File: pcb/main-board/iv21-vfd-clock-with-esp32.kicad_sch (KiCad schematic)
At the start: 30 parts, among them J1 Conn_02x10_Odd_Even, J2 4328, J4 Barrel_Jack_MountingPin, Q3 MMBT3904, Q4 MMBT3904, SW1 SW_SPST, SW2 SW_SPST, U1 MAX6921AQI_, U2 MOUDLE-SEEEDUINO-XIAO-ESP32C3, U4 MCP3221, U6 AZ1117-5.0

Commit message: PDF of schematic.
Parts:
- removed R1: 10K, Resistor_SMD:R_0805_2012Metric_Pad1.20x1.40mm_HandSolder, symbol Device:R_US
- R8: value 62 -> 2K
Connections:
- net at U2.3 (PA10_A2_D2): now also Q4.1 (B)
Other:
- moved on the sheet: C1, C2
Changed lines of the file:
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@@
 	)
 	(junction
-		(at 208.28 21.59)
+		(at 143.51 171.45)
 		(diameter 0)
 		(color 0 0 0 0)
 	)
 	(junction
-		(at 144.78 171.45)
+		(at 208.28 21.59)
 		(diameter 0)
 		(color 0 0 0 0)
@@
 	)
 	(junction
-		(at 139.7 171.45)
+		(at 156.21 171.45)
 		(diameter 0)
 		(color 0 0 0 0)
 	)
 	(junction
-		(at 151.13 171.45)
+		(at 148.59 171.45)
 		(diameter 0)
 		(color 0 0 0 0)
@@
 	(wire
 		(pts
+			(xy 143.51 171.45) (xy 148.59 171.45)
+		)
+		(stroke
+			(width 0)
+			(type default)
+		)
+	)
+	(wire
+		(pts
 			(xy 41.91 68.58) (xy 67.31 68.58)
 		)
@@
 	(wire
 		(pts
-			(xy 146.05 161.29) (xy 151.13 161.29)
+			(xy 146.05 161.29) (xy 156.21 161.29)
 		)
 		(stroke
@@
 	(wire
 		(pts
-			(xy 41.91 128.27) (xy 143.51 128.27)
+			(xy 41.91 128.27) (xy 152.4 128.27)
 		)
 		(stroke
@@
 	(wire
 		(pts
-			(xy 151.13 171.45) (xy 151.13 161.29)
+			(xy 156.21 171.45) (xy 156.21 161.29)
 		)
 		(stroke
@@
 	(wire
 		(pts
-			(xy 127 171.45) (xy 139.7 171.45)
+			(xy 127 171.45) (xy 143.51 171.45)
 		)
 		(stroke
@@
 	(wire
 		(pts
-			(xy 227.33 85.09) (xy 231.14 85.09)
+			(xy 148.59 171.45) (xy 156.21 171.45)
 		)
 		(stroke
@@
 	(wire
 		(pts
-			(xy 116.84 60.96) (xy 120.65 60.96)
+			(xy 227.33 85.09) (xy 231.14 85.09)
 		)
 		(stroke
@@
 	(wire
 		(pts
-			(xy 194.31 64.77) (xy 177.8 64.77)
+			(xy 116.84 60.96) (xy 120.65 60.96)
 		)
 		(stroke
@@
 	(wire
 		(pts
-			(xy 55.88 96.52) (xy 134.62 96.52)
+			(xy 194.31 64.77) (xy 177.8 64.77)
 		)
 		(stroke
@@
 	(wire
 		(pts
-			(xy 64.77 43.18) (xy 63.5 43.18)
+			(xy 55.88 96.52) (xy 134.62 96.52)
 		)
 		(stroke
@@
 	(wire
 		(pts
-			(xy 104.14 139.7) (xy 114.3 139.7)
+			(xy 64.77 43.18) (xy 63.5 43.18)
 		)
 		(stroke
@@
 	(wire
 		(pts
-			(xy 58.42 80.01) (xy 67.31 80.01)
+			(xy 104.14 139.7) (xy 114.3 139.7)
 		)
 		(stroke
@@
 	(wire
 		(pts
-			(xy 152.4 128.27) (xy 151.13 128.27)
+			(xy 58.42 80.01) (xy 67.31 80.01)
 		)
 		(stroke
@@
 	(wire
 		(pts
-			(xy 151.13 171.45) (xy 144.78 171.45)
-		)
-		(stroke
-			(width 0)
-			(type default)
-		)
-	)
-	(wire
-		(pts
 			(xy 33.02 83.82) (xy 33.02 88.9)
 		)
@@
 	(wire
 		(pts
-			(xy 144.78 163.83) (xy 144.78 171.45)
+			(xy 148.59 163.83) (xy 148.59 171.45)
 		)
 		(stroke
@@
 	(wire
 		(pts
-			(xy 139.7 171.45) (xy 144.78 171.45)
-		)
-		(stroke
-			(width 0)
-			(type default)
-		)
-	)
-	(wire
-		(pts
 			(xy 16.51 63.5) (xy 16.51 69.85)
 		)
@@
 	(wire
 		(pts
-			(xy 144.78 163.83) (xy 143.51 163.83)
-		)
-		(stroke
-			(width 0)
-			(type default)
-		)
-	)
-	(wire
-		(pts
 			(xy 234.95 72.39) (xy 234.95 52.07)
 		)
@@
 	)
 	(label "VPP"
-		(at 144.78 166.37 0)
+		(at 148.59 166.37 0)
 		(effects
 			(font
@@
 			)
 		)
-		(property "Value" "62"
+		(property "Value" "2K"
 			(at 255.27 58.4199 0)
 			(effects
@@
 	(symbol
 		(lib_id "Device:C_Polarized_US")
-		(at 139.7 175.26 0)
+		(at 143.51 175.26 0)
 		(unit 1)
 		(exclude_from_sim no)
@@
 		(dnp no)
 		(property "Reference" "C1"
-			(at 142.494 173.99 0)
+			(at 146.304 173.99 0)
 			(effects
 				(font
@@
 		)
 		(property "Value" "33uF"
-			(at 142.494 176.53 0)
+			(at 146.304 176.53 0)
 			(effects
 				(font
@@
 		)
 		(property "Footprint" "Capacitor_SMD:CP_Elec_8x10.5"
-			(at 139.7 175.26 0)
+			(at 143.51 175.26 0)
 			(effects
 				(font
@@
 		)
 		(property "Datasheet" "~"
-			(at 139.7 175.26 0)
+			(at 143.51 175.26 0)
 			(effects
 				(font
@@
 		)
 		(property "Description" "Polarized capacitor, US symbol"
-			(at 139.7 175.26 0)
+			(at 143.51 175.26 0)
 			(effects
 				(font
@@
 	(symbol
 		(lib_id "power:GND")
-		(at 151.13 179.07 0)
+		(at 156.21 179.07 0)
 		(unit 1)
 		(exclude_from_sim no)
@@
 		(fields_autoplaced yes)
 		(property "Reference" "#PWR010"
-			(at 151.13 185.42 0)
+			(at 156.21 185.42 0)
 			(effects
 				(font
@@
 		)
 		(property "Value" "GND"
-			(at 151.13 184.15 0)
+			(at 156.21 184.15 0)
 			(effects
 				(font
@@
 		)
 		(property "Footprint" ""
-			(at 151.13 179.07 0)
+			(at 156.21 179.07 0)
 			(effects
 				(font
@@
 		)
 		(property "Datasheet" ""
-			(at 151.13 179.07 0)
+			(at 156.21 179.07 0)
 			(effects
 				(font
@@
 		)
 		(property "Description" "Power symbol creates a global label with name \"GND\" , ground"
-			(at 151.13 179.07 0)
+			(at 156.21 179.07 0)
 			(effects
 				(font
@@
 	(symbol
 		(lib_id "power:GND")
-		(at 139.7 179.07 0)
+		(at 143.51 179.07 0)
 		(unit 1)
 		(exclude_from_sim no)
@@
 		(fields_autoplaced yes)
 		(property "Reference" "#PWR09"
-			(at 139.7 185.42 0)
+			(at 143.51 185.42 0)
 			(effects
 				(font
@@
 		)
 		(property "Value" "GND"
-			(at 139.7 184.15 0)
+			(at 143.51 184.15 0)
 			(effects
 				(font
@@
 		)
 		(property "Footprint" ""
-			(at 139.7 179.07 0)
+			(at 143.51 179.07 0)
 			(effects
 				(font
@@
 		)
 		(property "Datasheet" ""
-			(at 139.7 179.07 0)
+			(at 143.51 179.07 0)
 			(effects
 				(font
@@
 		)
 		(property "Description" "Power symbol creates a global label with name \"GND\" , ground"
-			(at 139.7 179.07 0)
+			(at 143.51 179.07 0)
 			(effects
 				(font
@@
 	)
 	(symbol
-		(lib_id "Device:R_US")
-		(at 147.32 128.27 90)
-		(unit 1)
-		(exclude_from_sim no)
-		(in_bom yes)
-		(on_board yes)
-		(dnp no)
-		(fields_autoplaced yes)
-		(property "Reference" "R1"
-			(at 147.32 121.92 90)
-			(effects
-				(font
-					(size 1.27 1.27)
-				)
-			)
-		)
-		(property "Value" "10K"
-			(at 147.32 124.46 90)
-			(effects
-				(font
-					(size 1.27 1.27)
-				)
-			)
-		)
-		(property "Footprint" "Resistor_SMD:R_0805_2012Metric_Pad1.20x1.40mm_HandSolder"
-			(at 147.574 127.254 90)
-			(effects
-				(font
-					(size 1.27 1.27)
-				)
-				(hide yes)
-			)
-		)
-		(property "Datasheet" "~"
-			(at 147.32 128.27 0)
-			(effects
-				(font
-					(size 1.27 1.27)
-				)
-				(hide yes)
-			)
-		)
-		(property "Description" "Resistor, US symbol"
-			(at 147.32 128.27 0)
-			(effects
-				(font
-					(size 1.27 1.27)
-				)
-				(hide yes)
-			)
-		)
-		(pin "1"
-		)
-		(pin "2"
-		)
-		(instances
-			(project ""
-				(path "/f4ccf12f-2c39-4319-adc8-75ef731d1807"
-					(reference "R1")
-					(unit 1)
-				)
-			)
-		)
-	)
-	(symbol
 		(lib_id "power:GND")
 		(at 29.21 55.88 0)
@@
 	(symbol
 		(lib_id "Device:C_Polarized_US")
-		(at 151.13 175.26 0)
+		(at 156.21 175.26 0)
 		(unit 1)
 		(exclude_from_sim no)
@@
 		(dnp no)
 		(property "Reference" "C2"
-			(at 154.432 173.99 0)
+			(at 159.512 173.99 0)
 			(effects
 				(font
@@
 		)
 		(property "Value" "0.1uF"
-			(at 154.432 176.276 0)
+			(at 159.512 176.276 0)
 			(effects
 				(font
@@
 		)
 		(property "Footprint" "Resistor_SMD:R_0805_2012Metric_Pad1.20x1.40mm_HandSolder"
-			(at 151.13 175.26 0)
+			(at 156.21 175.26 0)
 			(effects
 				(font
@@
 		)
 		(property "Datasheet" "~"
-			(at 151.13 175.26 0)
+			(at 156.21 175.26 0)
 			(effects
 				(font
@@
 		)
 		(property "Description" "Polarized capacitor, US symbol"
-			(at 151.13 175.26 0)
+			(at 156.21 175.26 0)
 			(effects
 				(font

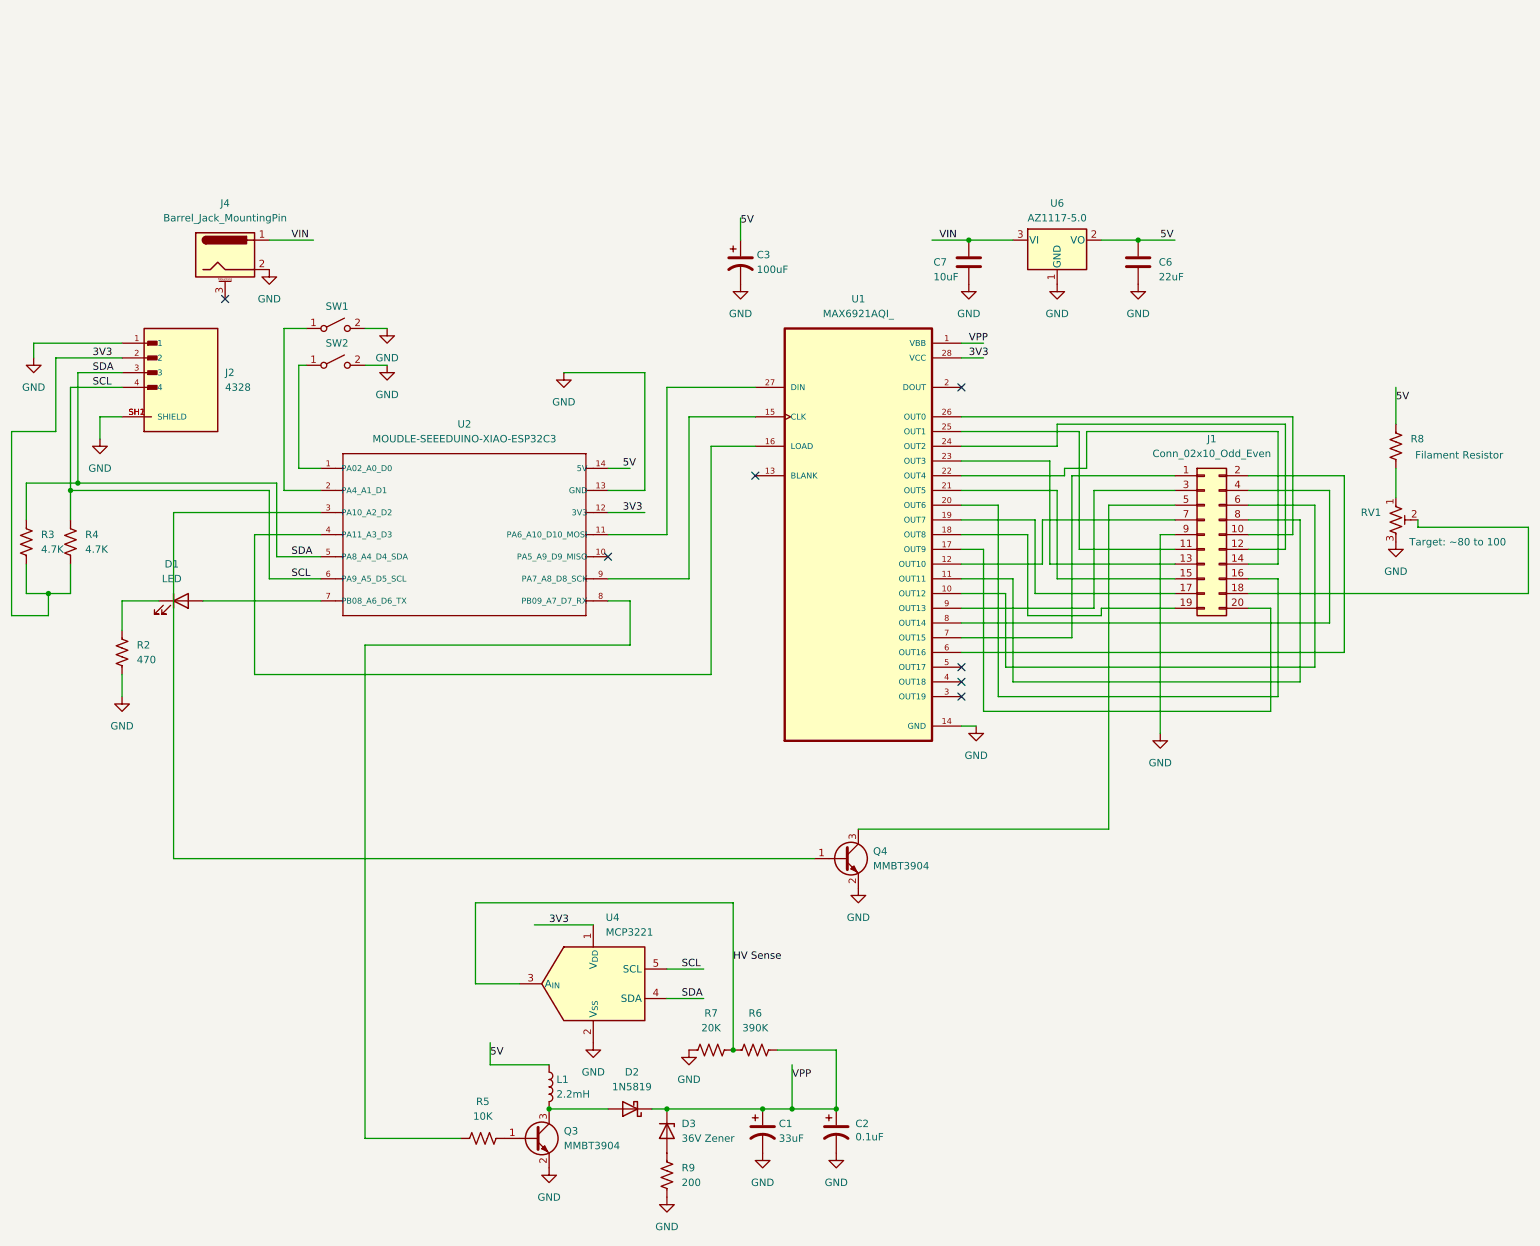
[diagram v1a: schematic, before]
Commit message: Voltage regulation update.
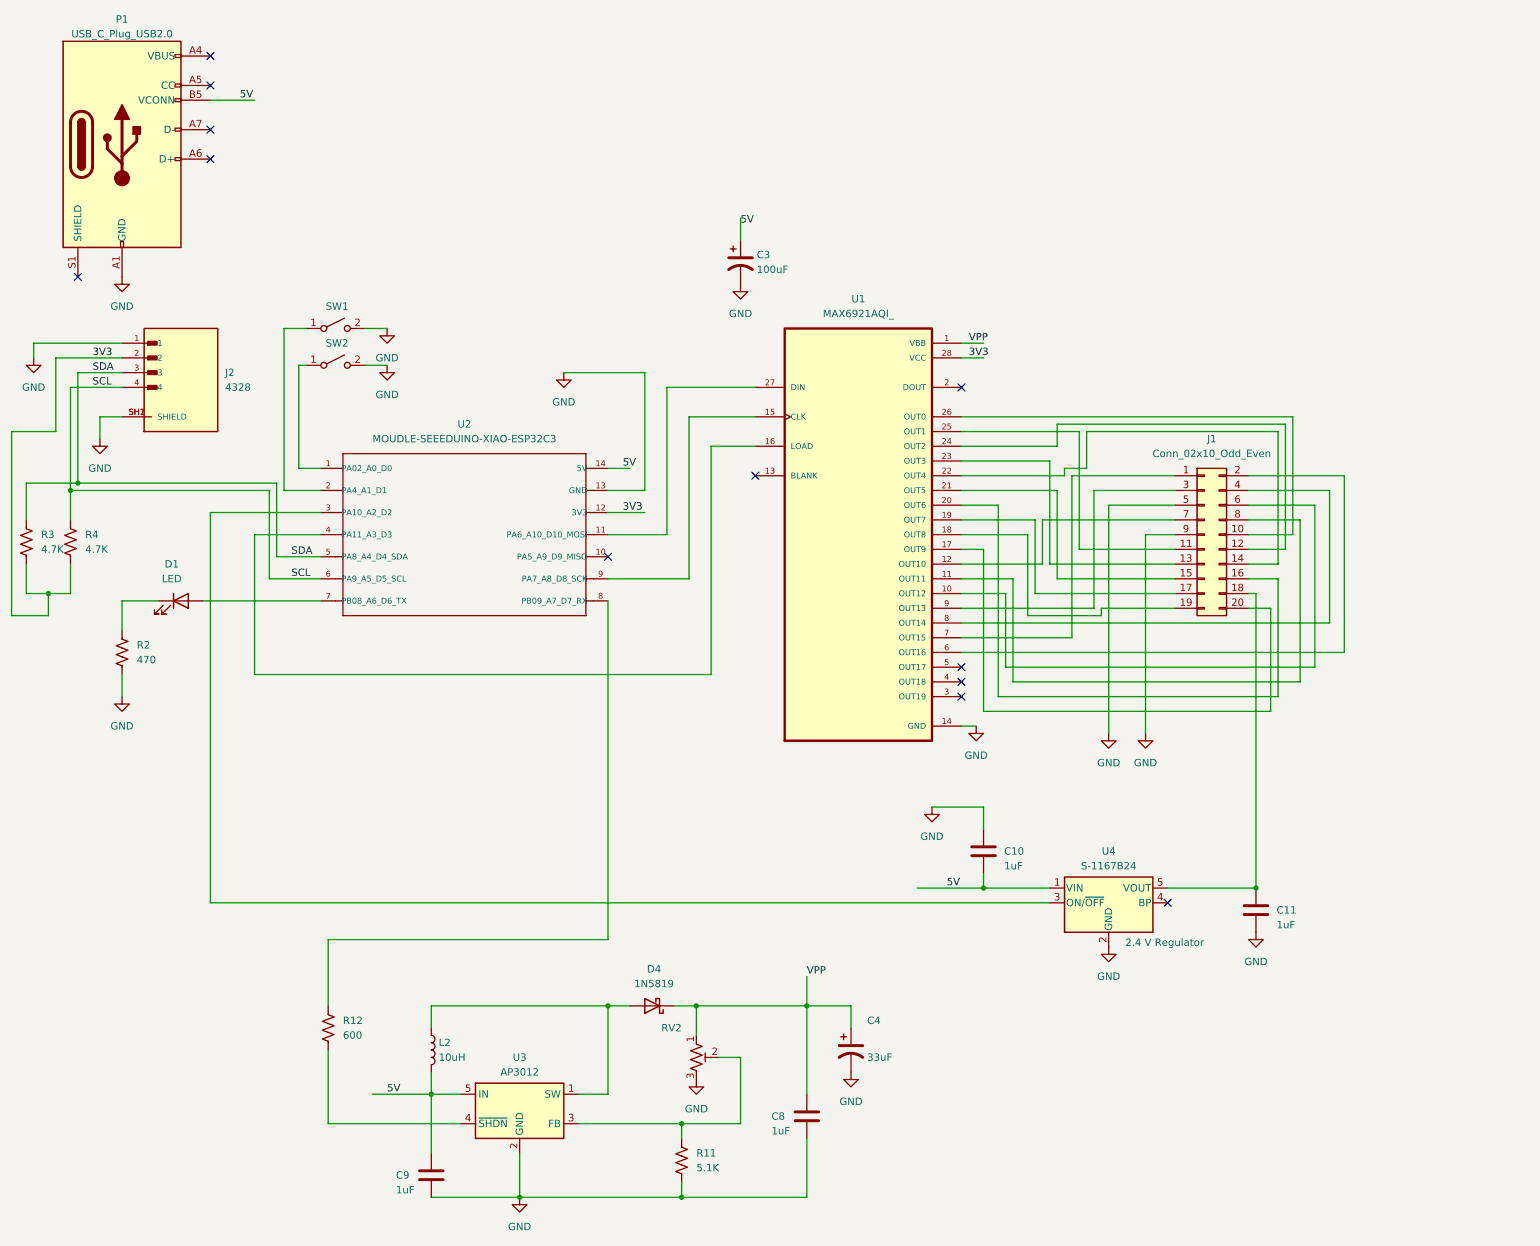
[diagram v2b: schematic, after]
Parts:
- removed C1: 33uF, Capacitor_SMD:CP_Elec_8x10.5, symbol Device:C_Polarized_US
- removed C2: 0.1uF, Resistor_SMD:R_0805_2012Metric_Pad1.20x1.40mm_HandSolder, symbol Device:C_Polarized_US
- removed C6: 22uF, Resistor_SMD:R_0805_2012Metric_Pad1.20x1.40mm_HandSolder, symbol Device:C
- removed C7: 10uF, Resistor_SMD:R_0805_2012Metric_Pad1.20x1.40mm_HandSolder, symbol Device:C
- removed D2: 1N5819, Diode_SMD:D_SOD-123, symbol Diode:1N5818
- removed D3: 36V Zener, Diode_SMD:D_SOD-128, symbol Device:D_Zener
- removed J4: Barrel_Jack_MountingPin, Connector_BarrelJack:BarrelJack_Wuerth_6941xx301002, symbol Connector:Barrel_Jack_MountingPin
- removed L1: 2.2mH, Inductor_THT:L_Radial_D12.0mm_P5.00mm_Fastron_11P, symbol Device:L
- removed Q3: MMBT3904, Package_TO_SOT_SMD:SOT-23-3, symbol Transistor_BJT:MMBT3904
- removed Q4: MMBT3904, Package_TO_SOT_SMD:SOT-23, symbol Transistor_BJT:MMBT3904
- removed R5: 10K, Resistor_SMD:R_0805_2012Metric_Pad1.20x1.40mm_HandSolder, symbol Device:R_US
- removed R6: 390K, Resistor_SMD:R_0805_2012Metric_Pad1.20x1.40mm_HandSolder, symbol Device:R_US
- removed R7: 20K, Resistor_SMD:R_0805_2012Metric_Pad1.20x1.40mm_HandSolder, symbol Device:R_US
- removed R8: 2K, Resistor_SMD:R_0805_2012Metric_Pad1.20x1.40mm_HandSolder, symbol Device:R_US
- removed R9: 200, Resistor_SMD:R_0805_2012Metric_Pad1.20x1.40mm_HandSolder, symbol Device:R_US
- removed RV1: 80, Potentiometer_THT:Potentiometer_Runtron_RM-065_Vertical, symbol Device:R_Potentiometer_Trim_US
- removed U4: MCP3221, Package_TO_SOT_SMD:SOT-23-5, symbol Analog_ADC:MCP3221
- removed U6: AZ1117-5.0, Package_TO_SOT_SMD:SOT-89-3_Handsoldering, symbol Regulator_Linear:AZ1117-5.0
- added C10, C11, C8, C9: 1uF, Resistor_SMD:R_0805_2012Metric_Pad1.20x1.40mm_HandSolder, symbol Device:C
- added C4: 33uF, Capacitor_SMD:CP_Elec_8x10.5, symbol Device:C_Polarized_US
- added D4: 1N5819, Diode_SMD:D_SOD-123, symbol Diode:1N5818
- added L2: 10uH, Inductor_THT:L_Radial_D12.0mm_P5.00mm_Fastron_11P, symbol Device:L
- added P1: USB_C_Plug_USB2.0, Connector_USB:USB_C_Receptacle_GCT_USB4105-xx-A_16P_TopMnt_Horizontal, symbol Connector:USB_C_Plug_USB2.0
- added R11: 5.1K, Resistor_SMD:R_0805_2012Metric_Pad1.20x1.40mm_HandSolder, symbol Device:R_US
- added R12: 600, Resistor_SMD:R_0805_2012Metric_Pad1.20x1.40mm_HandSolder, symbol Device:R_US
- added RV2: 100K, Potentiometer_THT:Potentiometer_Vishay_T93XA_Horizontal, symbol Device:R_Potentiometer_Trim_US
- added U3: AP3012, Package_TO_SOT_SMD:SOT-23-5, symbol Regulator_Switching:AP3012
- added U4: S-1167B24, Package_TO_SOT_SMD:SOT-23-5, symbol Regulator_Linear:LP2985-1.8
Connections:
- net 5V: now also C10.2, C9.1, L2.2, P1.B5 (VCONN), U3.5 (IN), U4.1 (VIN)
- net GND: now also J1.5 (Pin_5), C10.1, C11.2, C4.2, C8.2, C9.2, P1.A1 (GND), P1.A12 (GND), P1.B1 (GND), P1.B12 (GND), R11.2, RV2.3, U3.2 (GND), U4.2 (GND)
- net VPP: now also C4.1, C8.1, D4.1 (K), RV2.1
- net at U2.8 (PB09_A7_D7_RX): now also R12.1
- net at J1.18 (Pin_18): now also C11.1, U4.5 (VOUT)
- net at U2.3 (PA10_A2_D2): now also U4.3 (ON/~{OFF})
- new net: R11.1, RV2.2, U3.3 (FB)
- new net: R12.2, U3.4 (~{SHDN})
- new net: D4.2 (A), L2.1, U3.1 (SW)
- new net: P1.A4 (VBUS), P1.A9 (VBUS), P1.B4 (VBUS), P1.B9 (VBUS)
- no-connect marks 7 -> 12
